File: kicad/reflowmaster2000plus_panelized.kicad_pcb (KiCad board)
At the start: 2 copper layers, 94.6 x 97.3 mm, 262 parts, among them P1 CONN_02X04, P2 230V, P3 Toaster, U1 TLC2272, U2 MOC3063, U3 BTA24

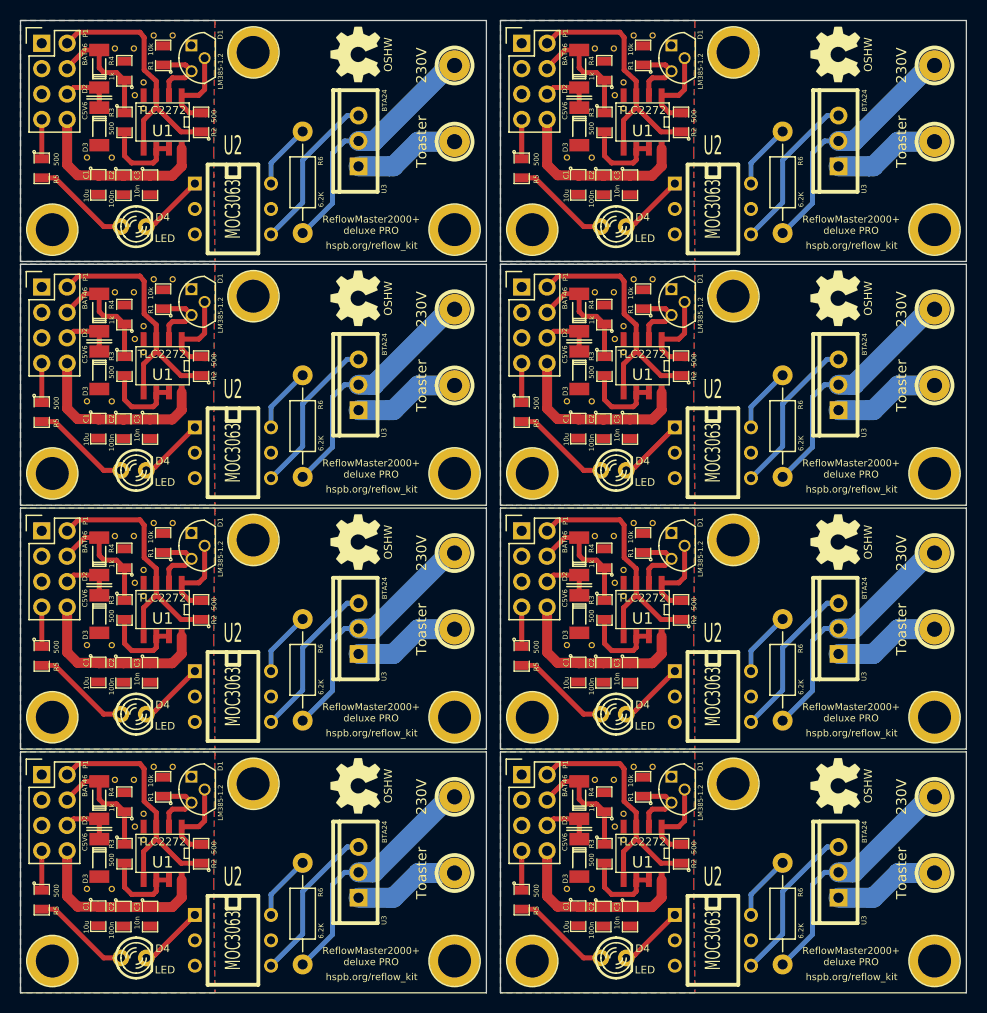
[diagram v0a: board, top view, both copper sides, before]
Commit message: [fix] gnd via not touching pad
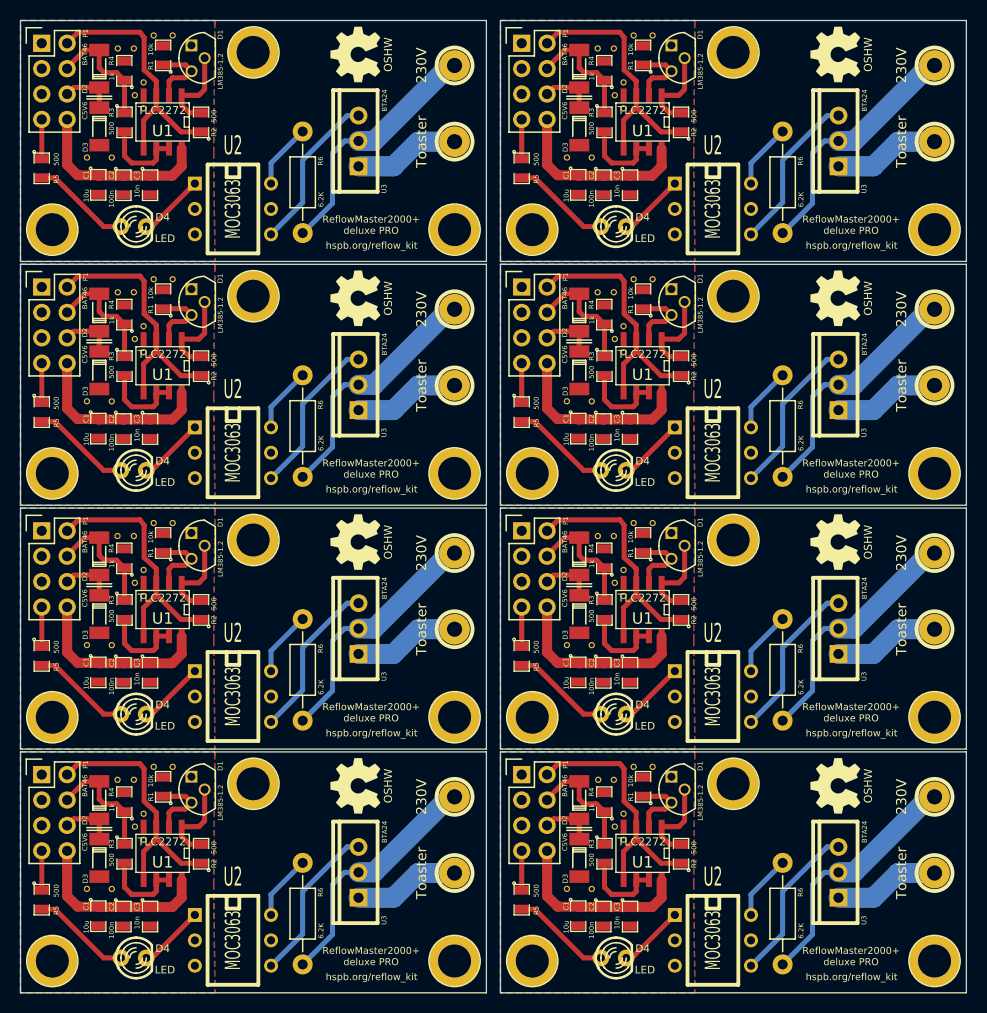
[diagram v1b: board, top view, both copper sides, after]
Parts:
- moved 1Pin_15mil_VIA 0.34 mm to (201.2, 157.5)
- moved 1Pin_15mil_VIA 0.30 mm to (201.2, 133.1)
- moved 1Pin_15mil_VIA 0.29 mm to (153.2, 108.7)
- moved 1Pin_15mil_VIA 0.29 mm to (153.2, 84.3)
- moved 1Pin_15mil_VIA 0.29 mm to (201.2, 84.3)
- moved 1Pin_15mil_VIA 0.28 mm to (201.2, 108.7)
- moved 1Pin_15mil_VIA 0.26 mm to (153.1, 157.5)
- moved 1Pin_15mil_VIA 0.26 mm to (153.1, 133.1)
